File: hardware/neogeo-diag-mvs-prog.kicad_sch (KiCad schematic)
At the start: 19 parts, among them J1 NeoGeo MVS Prog B Side Edge, J2 NeoGeo MVS Prog A Side Edge, J3 NeoGeo MVS Prog B Side Edge, J4 NeoGeo MVS Prog A Side Edge, U1 AS6C8016, U2 74LS11, U3 74LS08, U4 74LS04

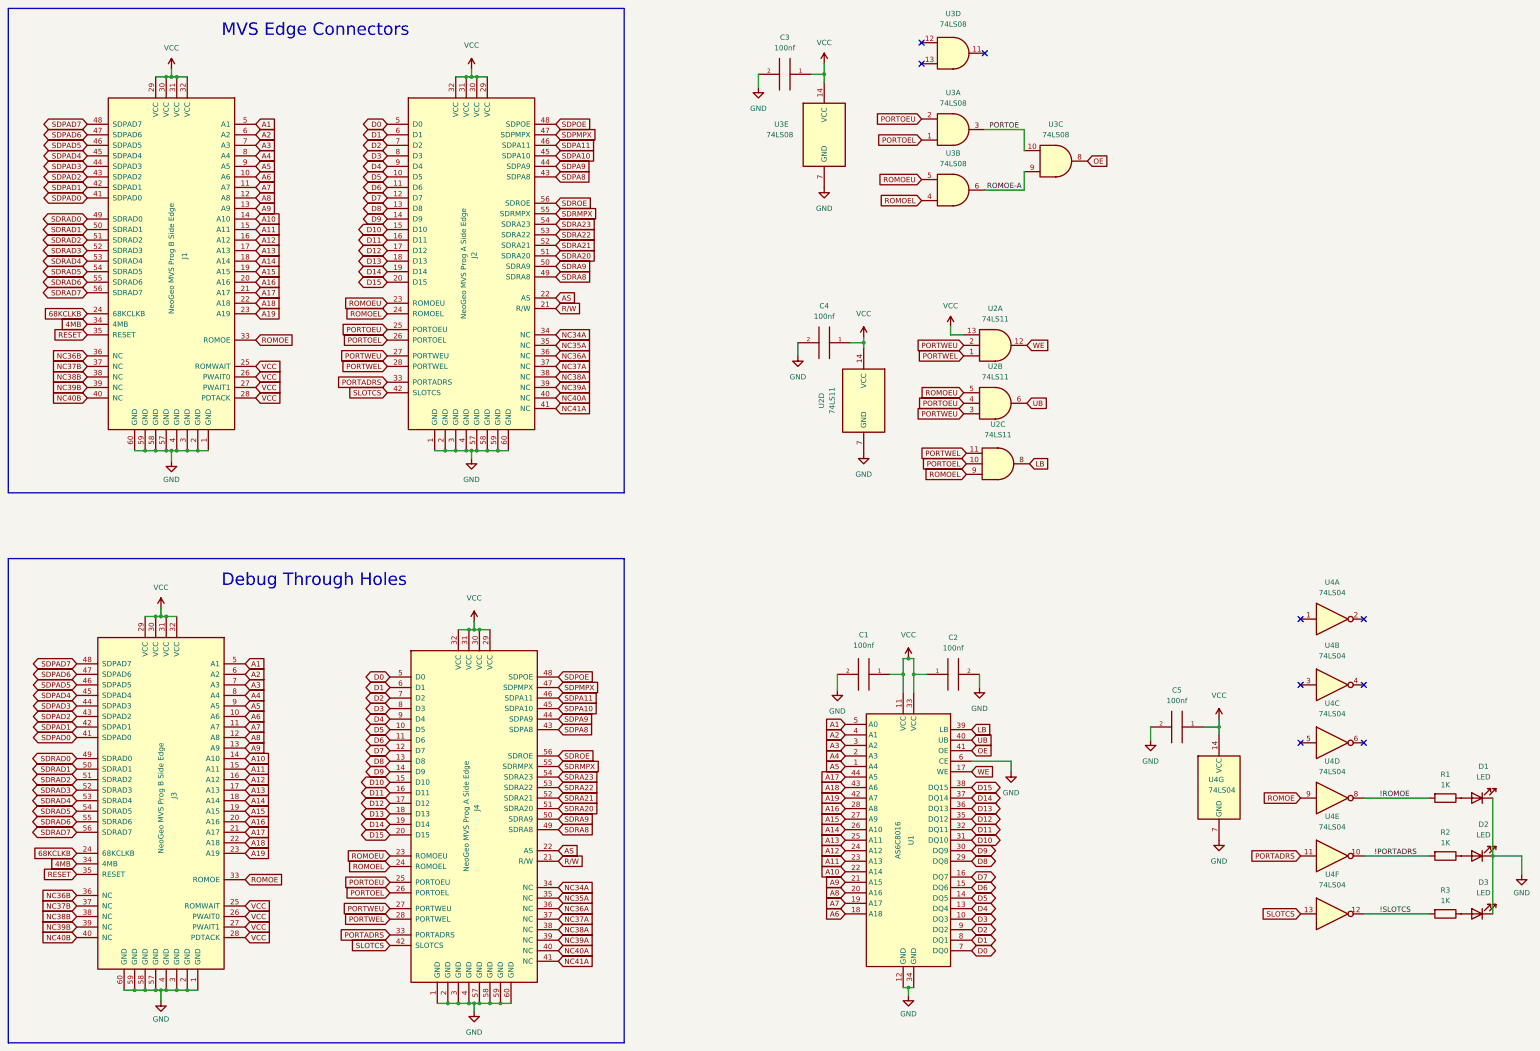
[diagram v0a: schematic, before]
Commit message: Fixes: directions in schematic, non-straight edge-cut
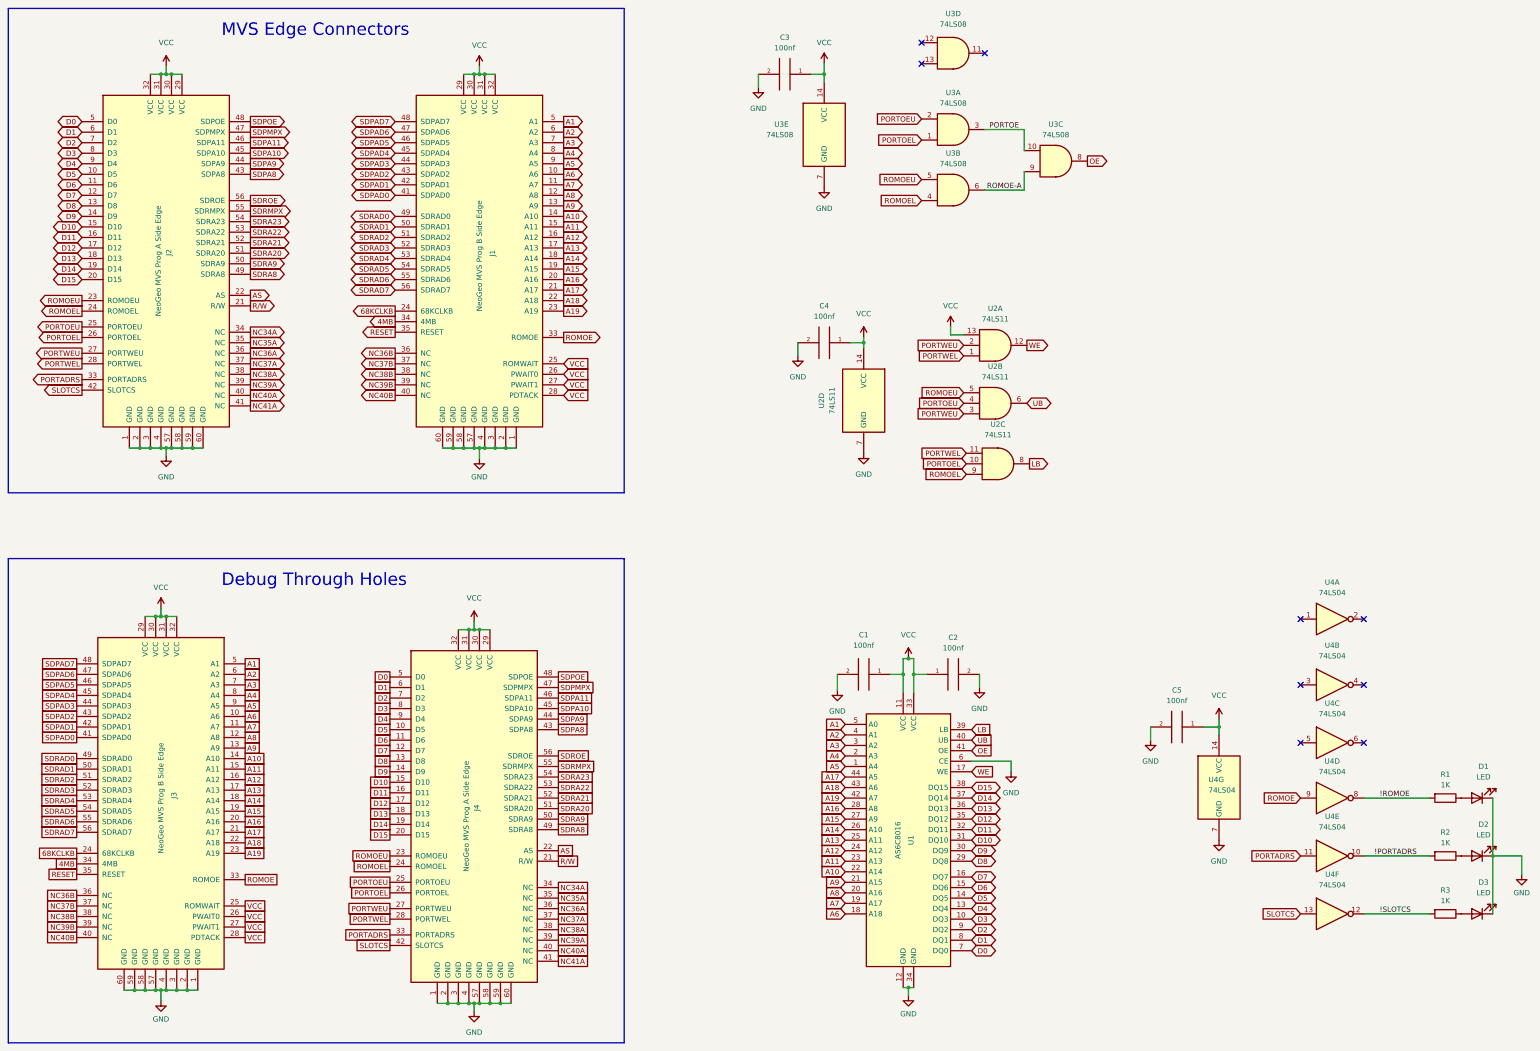
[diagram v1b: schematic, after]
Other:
- moved on the sheet: J1, J2
